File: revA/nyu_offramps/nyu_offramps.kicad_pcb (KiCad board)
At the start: 4 copper layers, 218 x 132 mm, 88 parts, among them J15 Conn_02x06_Odd_Even, J16 Conn_01x24_Female, J17 Conn_01x24_Female, J19 Conn_01x06_Male, J23 Screw_Terminal_01x02, J24 Conn_01x03_Male, J25 Screw_Terminal_01x02, J3 Conn_01x04_Pin, J4 Conn_01x01, U1 MCP4725xxx-xCH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

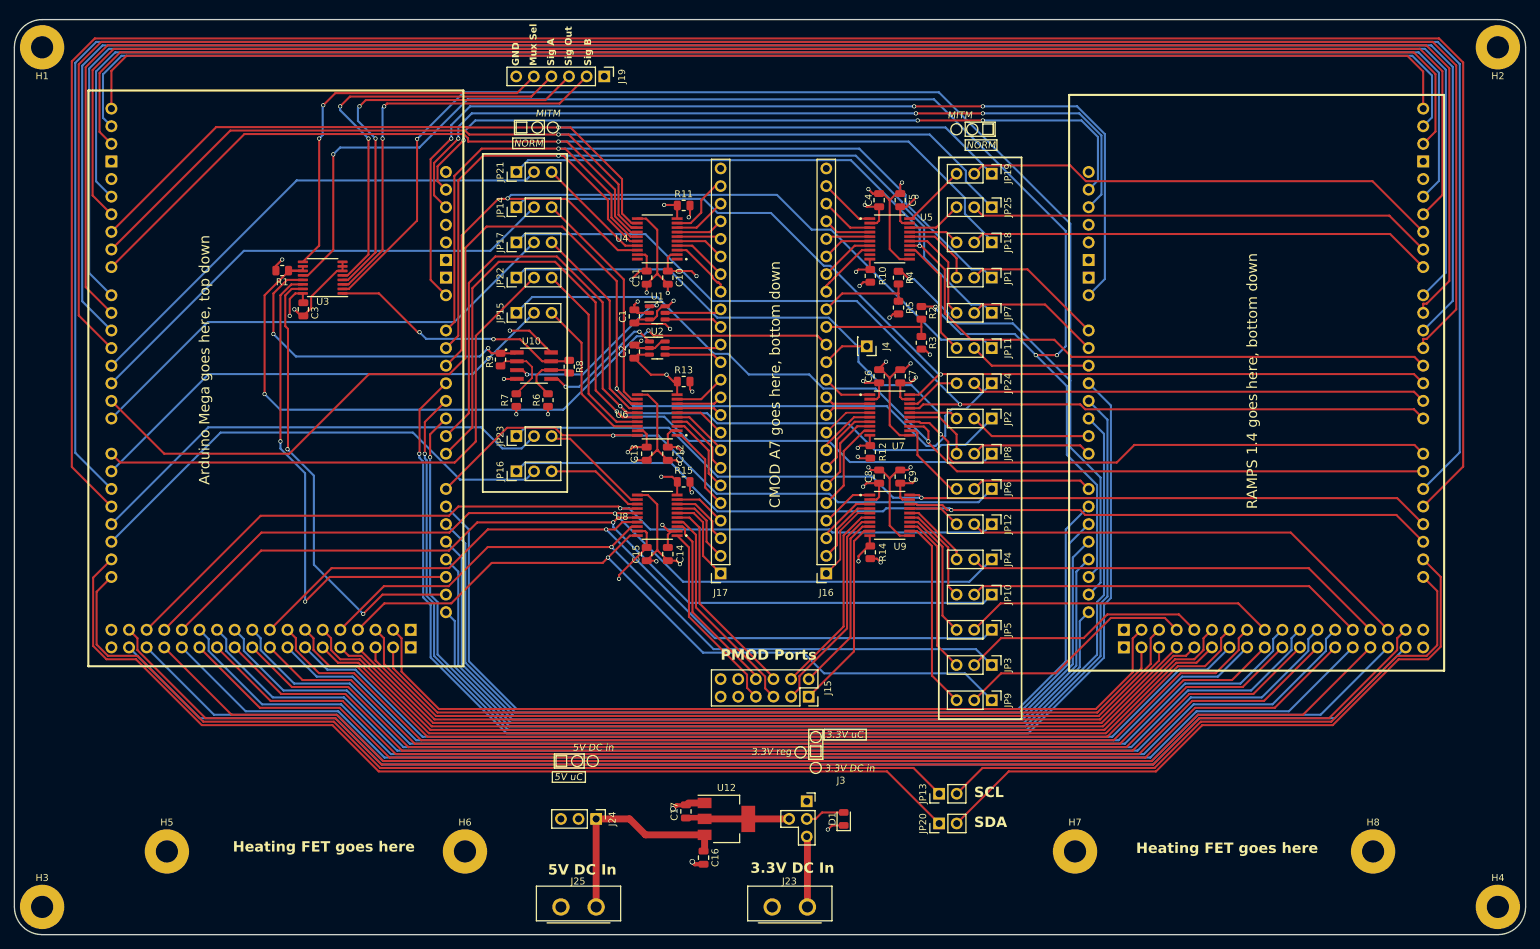
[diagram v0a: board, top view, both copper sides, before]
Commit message: Cleaned up and renamed project
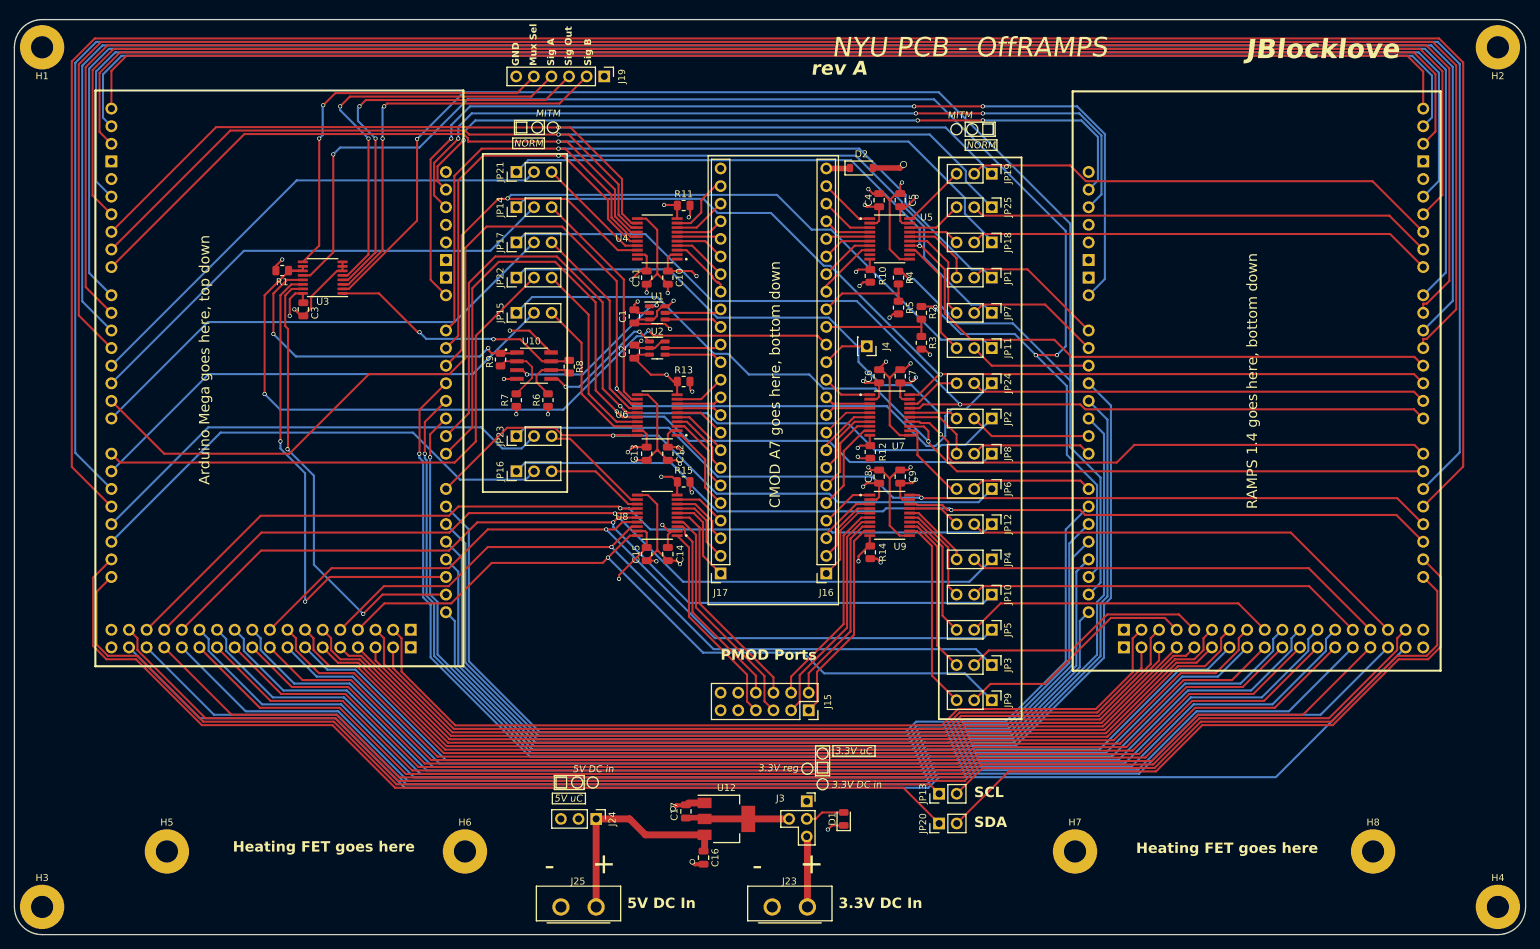
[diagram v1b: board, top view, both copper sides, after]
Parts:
- added D2: B5819W, Diode_SMD:D_SOD-123, F.Cu at (312.2, 89.4)
- moved J15 1.96 mm to (304.6, 167.6)
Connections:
- J16 pad 24: /5V_sel -> Net-(D2-K)
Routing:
- net /5V_sel: track 128.2 -> 115.2 mm, vias 8 -> 9
- net Net-(D2-K): track 0.00 -> 3.43 mm
- net /43: track 144.0 -> 146.8 mm
- net /A9: track 139.2 -> 142.0 mm
- net /THERM2: track 113.7 -> 116.5 mm
- net /A3: track 189.3 -> 192.1 mm
- net /A10: track 135.4 -> 138.2 mm
- net /32: track 175.2 -> 178.0 mm
- net /E1-EN: track 180.7 -> 183.5 mm
- net /E1-DIR: track 169.7 -> 172.5 mm
- net /41: track 149.5 -> 152.3 mm
- net /29: track 182.1 -> 184.9 mm
- net /E1-STEP: track 164.2 -> 167.0 mm
- net /A5: track 174.5 -> 177.3 mm
- net /A11: track 131.5 -> 134.3 mm
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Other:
- board text added: "+"
- board text added: "-"
- board text added: "JBlocklove"
- board text added: "NYU PCB - OffRAMPS"
- board text added: "rev A"
